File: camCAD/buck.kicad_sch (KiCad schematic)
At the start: 8 parts, among them J1 USB C Charging Port, J3 BATTERY, SW3 Power_SW, U1 BQ24072RGTR Charging IC, U2 SC189ZSKTRT

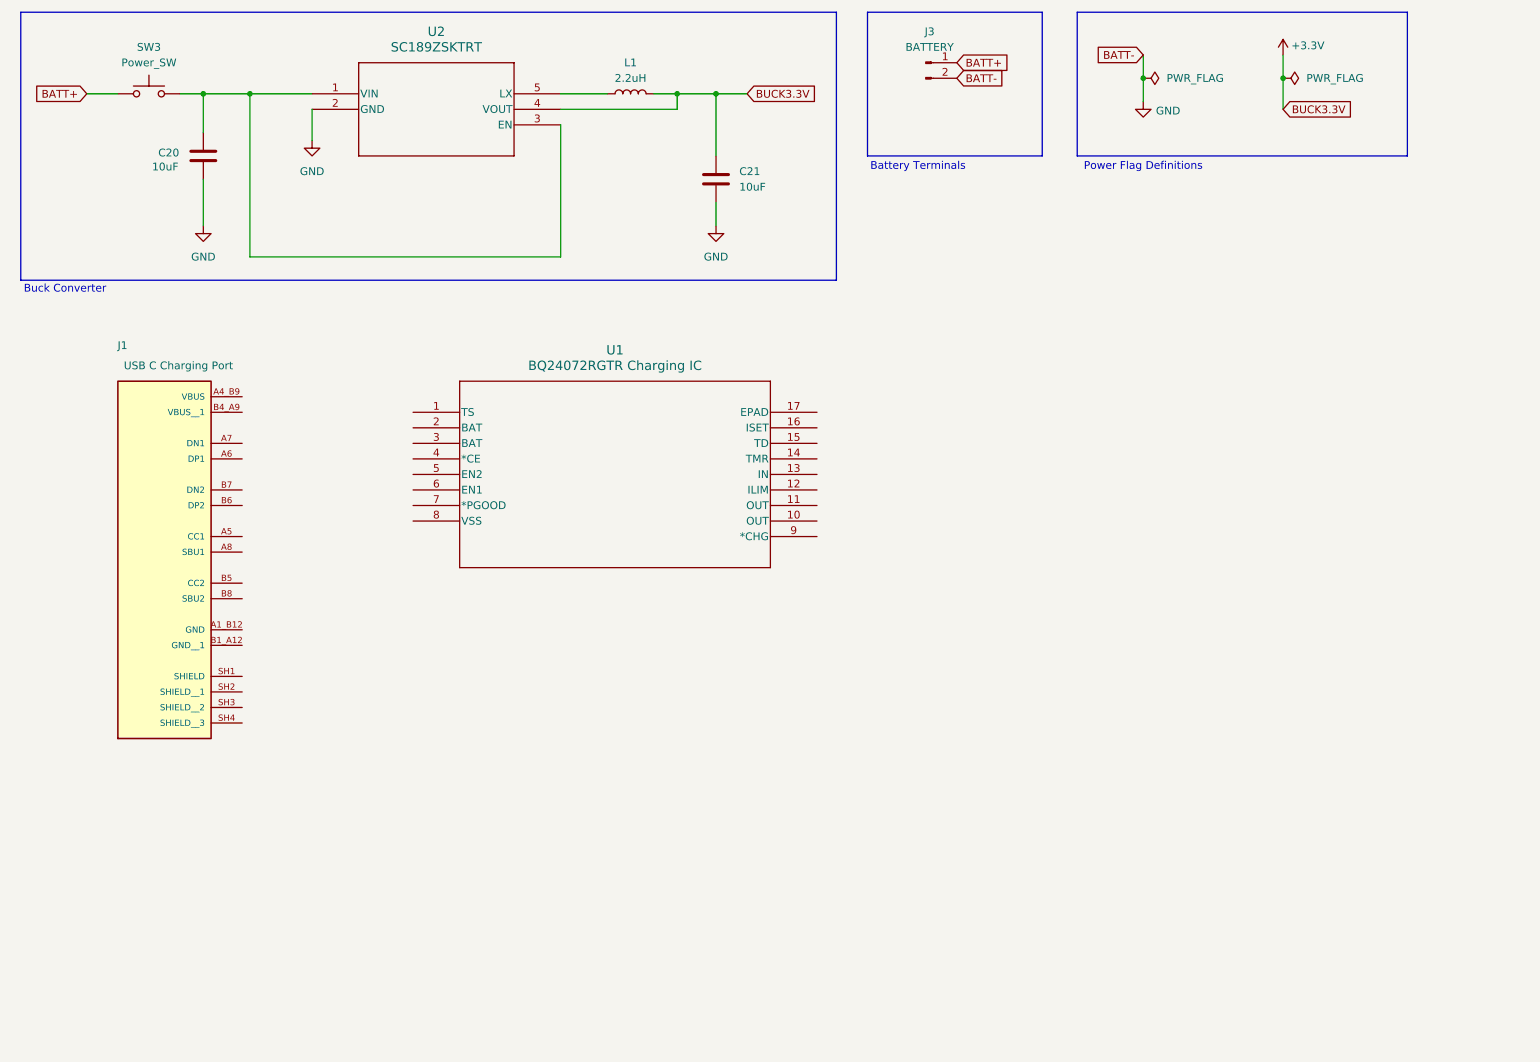
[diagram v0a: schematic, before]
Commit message: Nearly done with DPPM connections, updated readme
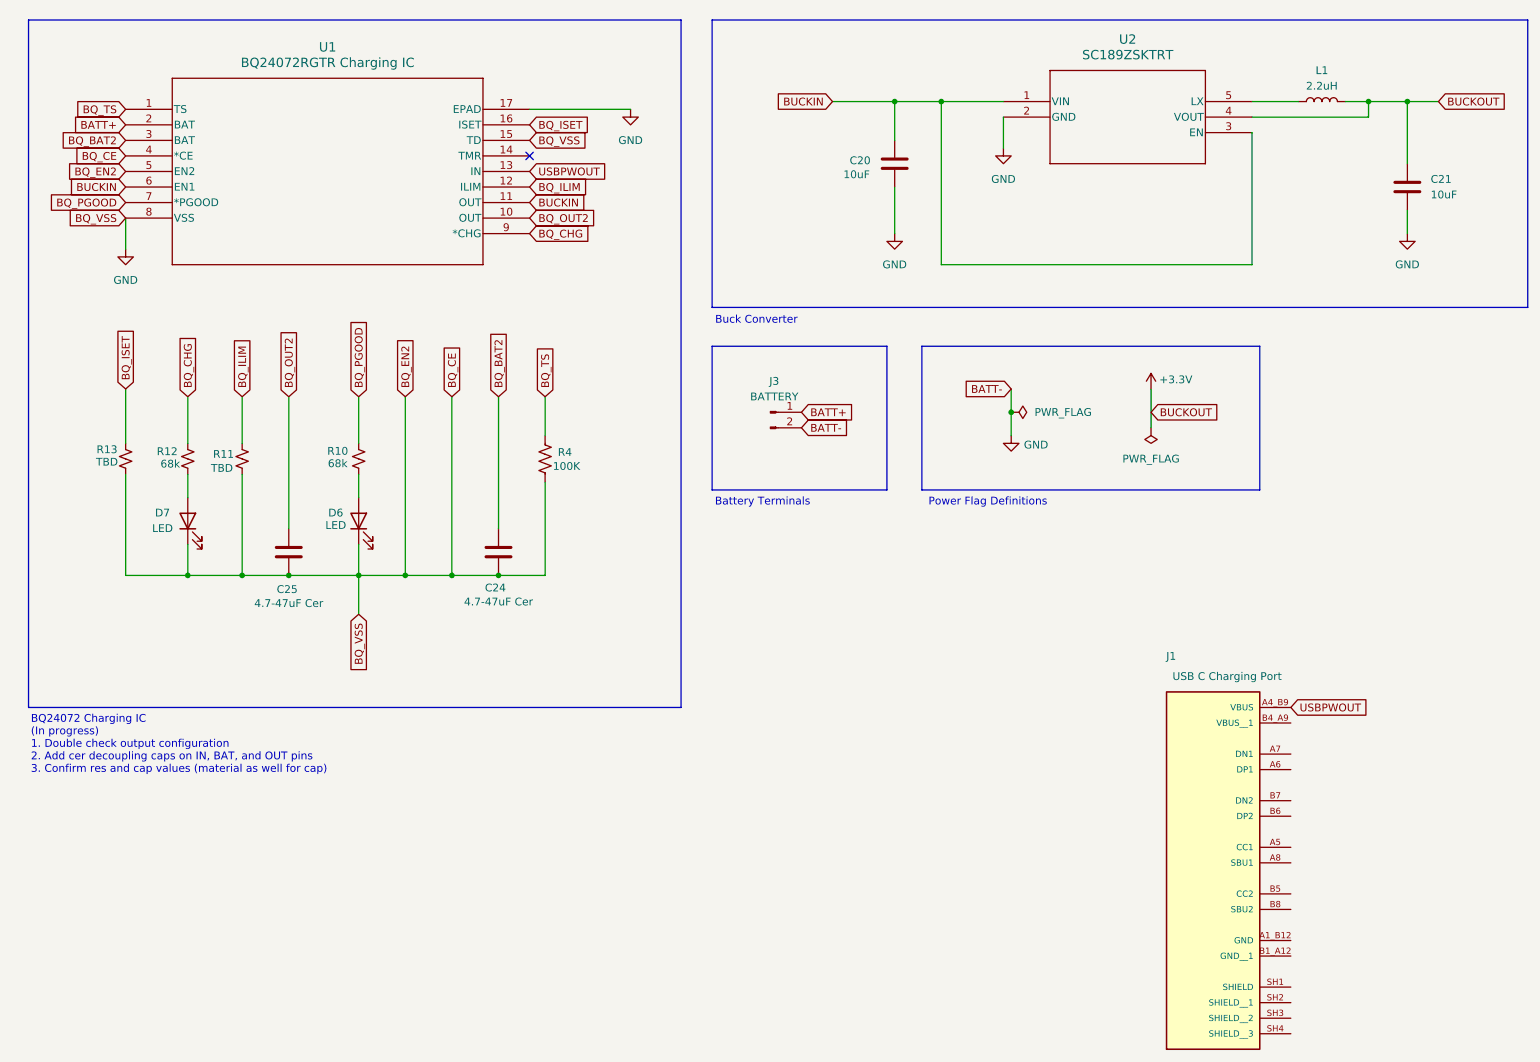
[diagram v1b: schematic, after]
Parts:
- removed SW3: Power_SW, symbol Switch:SW_Push
- added C24, C25: 4.7-47uF Cer, symbol Device:C
- added D6, D7: LED, symbol Device:LED
- added R10, R12: 68k, symbol Device:R_Small_US
- added R11, R13: TBD, symbol Device:R_Small_US
- added R4: 100K, symbol Device:R_US
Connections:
- net BATT+: now also U1.2 (BAT)
- net GND: now also U1.15 (TD), U1.17 (EPAD), U1.4 (*CE), U1.5 (EN2), U1.8 (VSS), C24.2, C25.2, D6.1 (K), D7.1 (K), R11.2, R13.2, R4.1
- net BQ_TS: now reaches U1.1 (TS)
- net BQ_TS: now also R4.2
- net BQ_OUT2: now reaches U1.10 (OUT)
- net BQ_OUT2: now also C25.1
- net BUCKIN: now reaches U1.11 (OUT)
- net BUCKIN: now also C20.1, U1.6 (EN1), U2.1 (VIN), U2.3 (EN)
- net BQ_ILIM: now reaches U1.12 (ILIM)
- net BQ_ILIM: now also R11.1
- net USBPWOUT: now reaches U1.13 (IN)
- net USBPWOUT: now also J1.A4_B9 (VBUS)
- net BQ_ISET: now reaches U1.16 (ISET)
- net BQ_ISET: now also R13.1
- net BQ_BAT2: now reaches U1.3 (BAT)
- net BQ_BAT2: now also C24.1
- net BQ_PGOOD: now reaches U1.7 (*PGOOD)
- net BQ_PGOOD: now also R10.1
- net BQ_CHG: now reaches U1.9 (*CHG)
- net BQ_CHG: now also R12.1
- new net: D6.2 (A), R10.2
- new net: D7.2 (A), R12.2
- no-connect marks 0 -> 1
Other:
- note added: "BQ24072 Charging IC (In progress) 1. Double check output configuration 2. Add cer decoupling caps on IN, BAT, and OUT pins 3. Confirm res and cap values (material as well for cap)"
- moved on the sheet: C20, C21, J1, J3, L1, U1, U2

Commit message: Completed charging schematic, updated readme
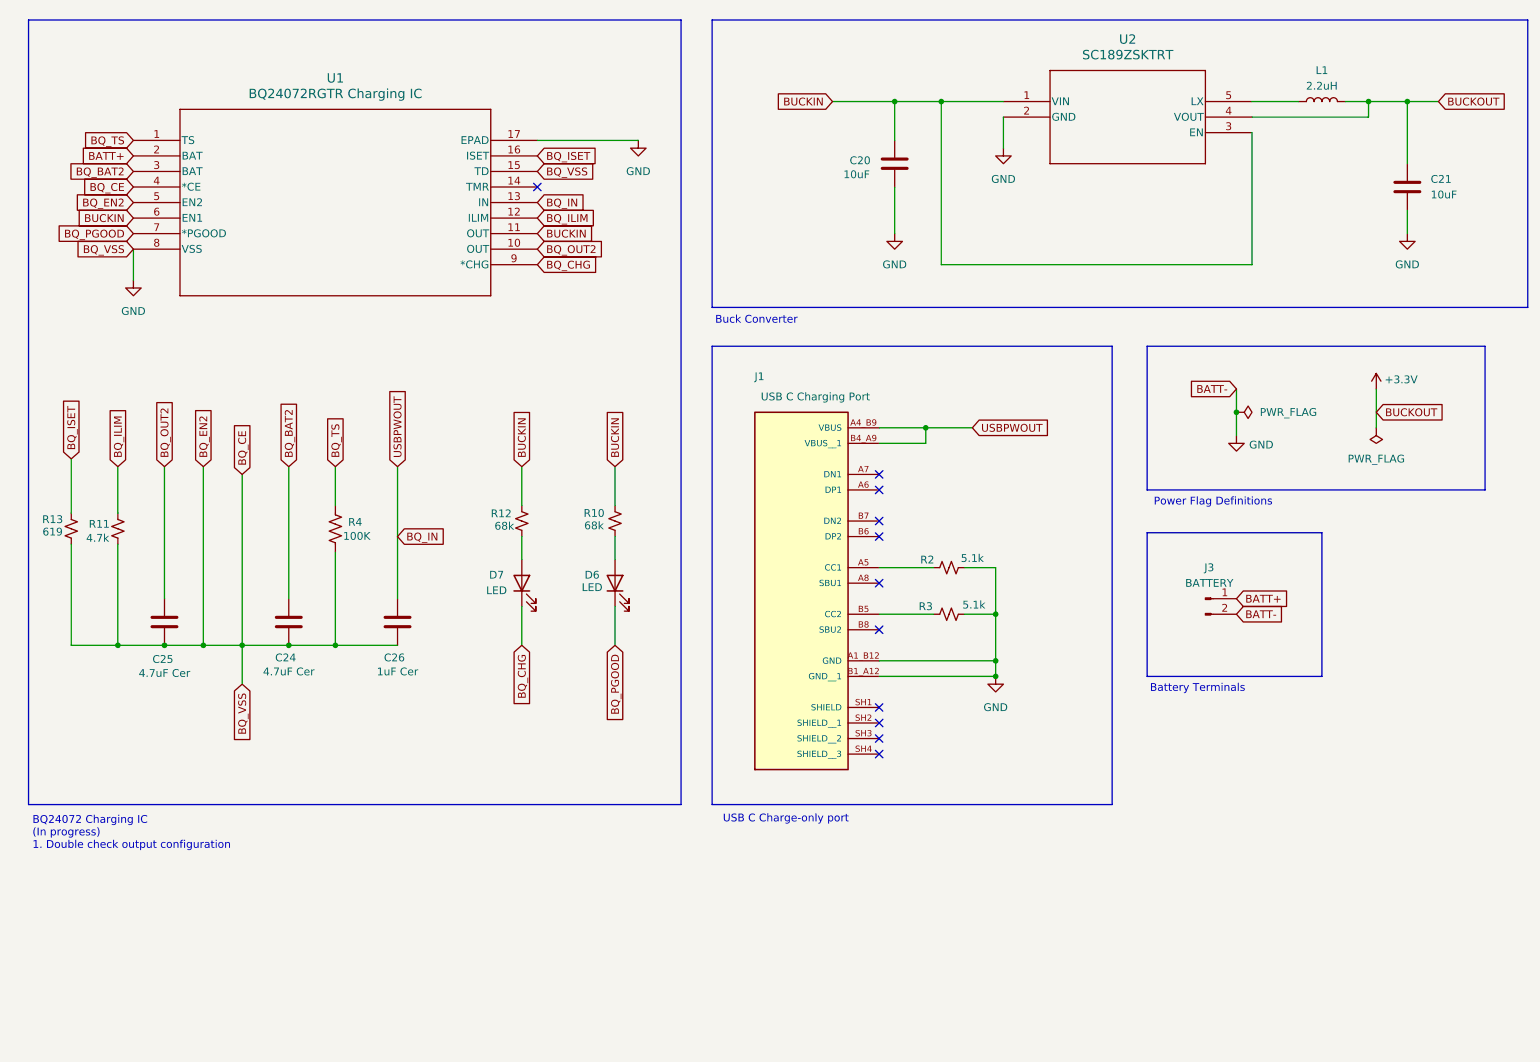
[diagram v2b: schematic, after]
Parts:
- added C26: 1uF Cer, symbol Device:C
- added R2, R3: 5.1k, symbol Device:R_Small_US
- C24, C25: value 4.7-47uF Cer -> 4.7uF Cer
- R11: value TBD -> 4.7k
- R13: value TBD -> 619
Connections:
- net USBPWOUT is gone; now on net BQ_IN: J1.A4_B9 (VBUS), U1.13 (IN)
- net BQ_CHG: now also D7.1 (K); no longer R12.1
- net BQ_PGOOD: now also D6.1 (K); no longer R10.1
- net BUCKIN: now also R10.1, R12.1
- net GND: now also J1.A1_B12 (GND), J1.B1_A12 (GND__1), C26.2, R2.2, R3.2; no longer D6.1 (K), D7.1 (K)
- net at J1.A5 (CC1): now also R2.1
- net BQ_IN: now reaches J1.B4_A9 (VBUS__1)
- net BQ_IN: now also C26.1
- net at J1.B5 (CC2): now also R3.1
- no-connect marks 1 -> 11
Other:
- note added: "BQ24072 Charging IC (In progress) 1. Double check output configuration"
- note added: "USB C Charge-only port"
- note removed: "BQ24072 Charging IC (In progress) 1. Double check output configuration 2. Add cer decoupling caps on IN, BAT, and OUT pins 3. Confirm res and cap values (material as well for cap)"
- title: Buck Converter 3.3V supply -> Power Supply and Charging Scheme
- moved on the sheet: C24, C25, J1, J3, R11, R13, R4, U1

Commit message: miscellaneous changes
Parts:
- R4: value 100K -> 10K
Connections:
- net BQ_OUT2: now also U1.6 (EN1)
- net +3.3V renamed SC_3V3
- net BUCKIN renamed BQ_OUT
- net BQ_OUT: no longer U1.6 (EN1)
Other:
- note added: "USB C Power-only port"
- note removed: "Power Flag Definitions"
- note removed: "USB C Charge-only port"
- moved on the sheet: C20, C21, J3, L1, R11, R13, U2

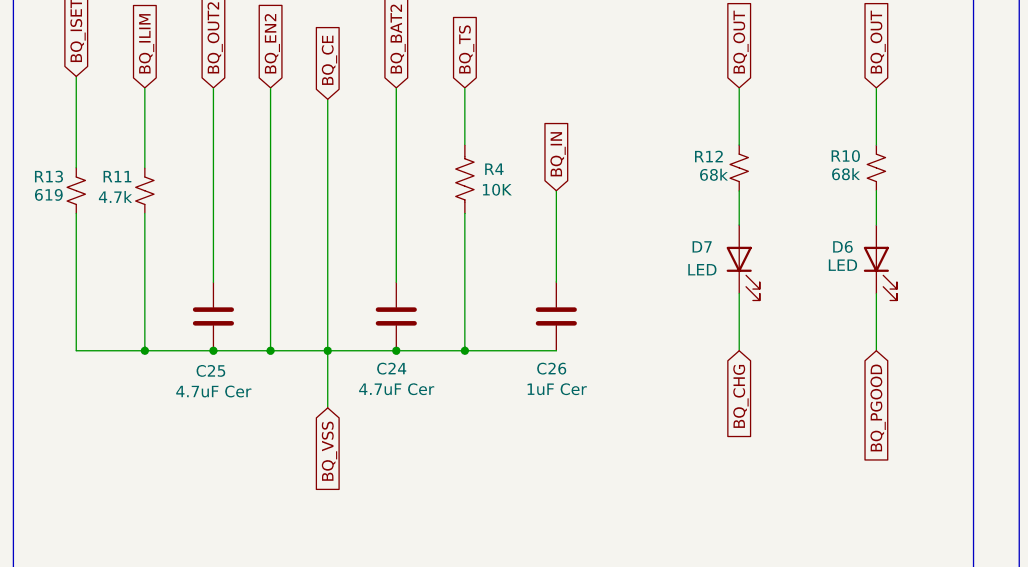
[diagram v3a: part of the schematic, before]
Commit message: Added footprints for major components, renamed some components for more specific information
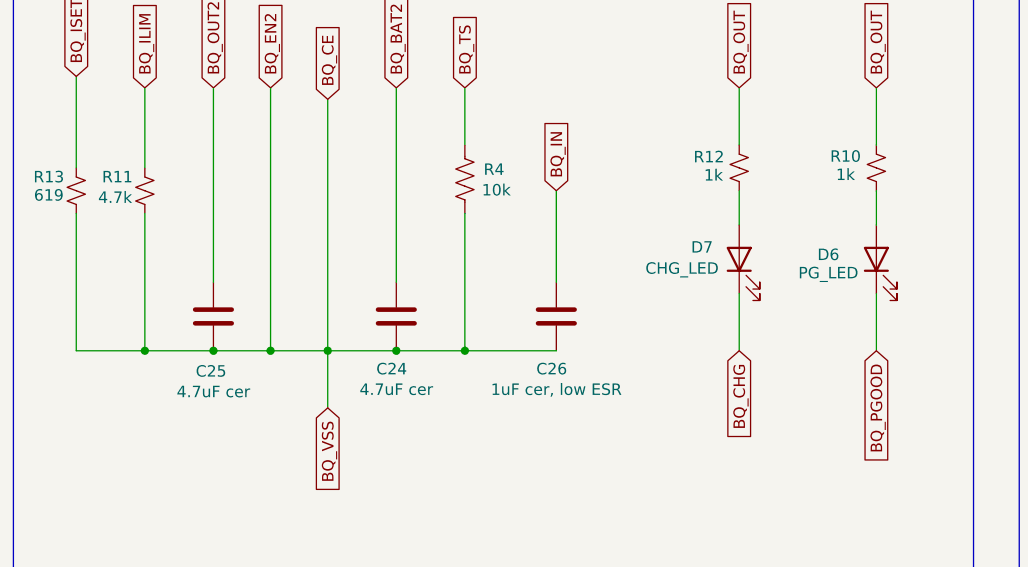
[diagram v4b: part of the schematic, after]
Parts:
- C24, C25: value 4.7uF Cer -> 4.7uF cer
- C26: value 1uF Cer -> 1uF cer, low ESR
- D6: value LED -> PG_LED; footprint (none) -> 1_LEDs:LEDM1608X80_G
- D7: value LED -> CHG_LED; footprint (none) -> 1_LEDs:LEDC1608X35N_R
- J1: footprint UJ20-C-H-G-SMT-1-P16-TR:SAMESKY_UJ20-C-H-G-SMT-1-P16-TR -> 1_Sockets:SAMESKY_UJ20-C-H-G-SMT-1-P16-TR
- J3: footprint (none) -> 1_Headers:JST_B2B-XH-A
- R10, R12: value 68k -> 1k
- R4: value 10K -> 10k
- U1: footprint RGT16_1P7X1P7 -> 1_DPPMs:RGT16_1P7X1P7
- U2: footprint SOT23-5-SC189_SEM -> 1_BuckConverters:SOT23-5-SC189_SEM
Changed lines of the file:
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@@
 			)
 		)
-		(property "Footprint" "RGT16_1P7X1P7"
+		(property "Footprint" "1_DPPMs:RGT16_1P7X1P7"
 			(at 34.29 36.83 0)
 			(hide yes)
@@
 		(dnp no)
 		(property "Reference" "D6"
-			(at 109.2835 107.8865 90)
-			(show_name no)
-			(do_not_autoplace no)
-			(effects
-				(font
-					(size 1.27 1.27)
-				)
-			)
-		)
-		(property "Value" "LED"
-			(at 109.2835 109.9185 90)
-			(show_name no)
-			(do_not_autoplace no)
-			(effects
-				(font
-					(size 1.27 1.27)
-				)
-			)
-		)
-		(property "Footprint" ""
+			(at 107.696 108.712 90)
+			(show_name no)
+			(do_not_autoplace no)
+			(effects
+				(font
+					(size 1.27 1.27)
+				)
+			)
+		)
+		(property "Value" "PG_LED"
+			(at 107.696 110.744 90)
+			(show_name no)
+			(do_not_autoplace no)
+			(effects
+				(font
+					(size 1.27 1.27)
+				)
+			)
+		)
+		(property "Footprint" "1_LEDs:LEDM1608X80_G"
 			(at 113.03 109.22 0)
 			(hide yes)
@@
 			)
 		)
-		(property "Value" "10K"
+		(property "Value" "10k"
 			(at 70.8025 101.5365 0)
 			(show_name no)
@@
 			)
 		)
-		(property "Value" "1uF Cer"
+		(property "Value" "1uF cer, low ESR"
 			(at 77.47 123.698 0)
 			(show_name no)
@@
 			)
 		)
-		(property "Value" "68k"
+		(property "Value" "1k"
 			(at 94.9325 99.8855 0)
 			(show_name no)
@@
 			)
 		)
-		(property "Value" "4.7uF Cer"
+		(property "Value" "4.7uF cer"
 			(at 59.69 123.698 0)
 			(show_name no)
@@
 			)
 		)
-		(property "Footprint" ""
+		(property "Footprint" "1_Headers:JST_B2B-XH-A"
 			(at 209.55 80.01 0)
 			(hide yes)
@@
 			)
 		)
-		(property "Value" "68k"
+		(property "Value" "1k"
 			(at 109.601 99.822 0)
 			(show_name no)
@@
 			)
 		)
-		(property "Footprint" "UJ20-C-H-G-SMT-1-P16-TR:SAMESKY_UJ20-C-H-G-SMT-1-P16-TR"
+		(property "Footprint" "1_Sockets:SAMESKY_UJ20-C-H-G-SMT-1-P16-TR"
 			(at 143.51 104.14 0)
 			(hide yes)
@@
 			)
 		)
-		(property "Value" "4.7uF Cer"
+		(property "Value" "4.7uF cer"
 			(at 39.37 123.952 0)
 			(show_name no)
@@
 			)
 		)
-		(property "Value" "LED"
-			(at 93.6625 110.4265 90)
-			(show_name no)
-			(do_not_autoplace no)
-			(effects
-				(font
-					(size 1.27 1.27)
-				)
-			)
-		)
-		(property "Footprint" ""
+		(property "Value" "CHG_LED"
+			(at 91.44 110.236 90)
+			(show_name no)
+			(do_not_autoplace no)
+			(effects
+				(font
+					(size 1.27 1.27)
+				)
+			)
+		)
+		(property "Footprint" "1_LEDs:LEDC1608X35N_R"
 			(at 97.79 109.22 0)
 			(hide yes)
@@
 			)
 		)
-		(property "Footprint" "SOT23-5-SC189_SEM"
+		(property "Footprint" "1_BuckConverters:SOT23-5-SC189_SEM"
 			(at 173.228 37.084 0)
 			(hide yes)
